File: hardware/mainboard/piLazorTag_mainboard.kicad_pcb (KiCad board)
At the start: 2 copper layers, 11 parts, among them M1 LOGIC_LEVEL_CONVERTER

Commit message: #9 More work on the mainboard
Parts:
- moved 5V_POWER1 14.0 mm to (163.8, 111.2)
- moved SSD1603 7.20 mm to (110.0, 121.6)
- moved INPUT1 6.60 mm to (150.6, 121.6)
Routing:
- net +5V: track 29.1 -> 136.6 mm
- net /IR_SIG: track 0.00 -> 50.9 mm
- net /LED_IR_GND: track 0.00 -> 20.2 mm
- net /M_LED_DI: track 0.58 -> 14.1 mm
- net /G2/i2c: track 15.8 -> 8.67 mm
- net /G3/i2c: track 15.8 -> 8.67 mm
- net /H_LED_DI: track 0.37 -> 7.48 mm
- net /G11/spi: track 17.6 -> 10.7 mm
- net /G19: track 15.3 -> 8.60 mm
- net /G6: track 15.3 -> 8.60 mm
- net /G5: track 15.3 -> 8.88 mm
- net /G26: track 15.3 -> 8.88 mm
- net /G13: track 15.3 -> 8.88 mm
- net Net-(100K1-Pad1): track 0.20 -> 6.06 mm
- net +3V3: track 96.2 -> 92.4 mm
- added copper zone on B.Cu, net GND
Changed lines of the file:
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@@
   (general
     (links 55)
-    (no_connects 36)
-    (area 0 0 0 0)
+    (no_connects 9)
+    (area 96.495 62.695238 167.205 133.833333)
     (thickness 1.6)
     (drawings 0)
-    (tracks 46)
+    (tracks 80)
     (zones 0)
     (modules 11)
@@
     (last_trace_width 1)
     (trace_clearance 0.2)
-    (zone_clearance 0.508)
+    (zone_clearance 0.6)
     (zone_45_only no)
     (trace_min 0.2)
@@
   )
   (module Pin_Headers:Pin_Header_Straight_2x01_Pitch2.54mm (layer F.Cu)
-    (at 163.8 125.2 270)
+    (at 163.8 111.2 270)
     (descr "Through hole straight pin header, 2x01, 2.54mm pitch, double rows")
     (tags "Through hole pin header THT 2x01 2.54mm double row")
@@
   )
   (module Pin_Headers:Pin_Header_Straight_1x08_Pitch2.54mm (layer F.Cu)
-    (at 150.8 128.2 270)
+    (at 150.6 121.6 270)
     (descr "Through hole straight pin header, 1x08, 2.54mm pitch, single row")
     (tags "Through hole pin header THT 1x08 2.54mm single row")
@@
   )
   (module Pin_Headers:Pin_Header_Straight_1x04_Pitch2.54mm (layer F.Cu)
-    (at 110 128.8 270)
+    (at 110 121.6 270)
     (descr "Through hole straight pin header, 1x04, 2.54mm pitch, single row")
     (tags "Through hole pin header THT 1x04 2.54mm single row")
@@
     )
   )
-  (segment (start 163.8 125.2) (end 163.8 96.52) (width 1) (layer B.Cu) (net 1))
+  (segment (start 163.8 111.2) (end 163.8 96.52) (width 1) (layer B.Cu) (net 1) (status C00000))
+  (segment (start 163.8 96.52) (end 163.49 96.21) (width 1) (layer B.Cu) (net 1) (status C00000))
+  (segment (start 112.51 88.17) (end 112.51 87.49) (width 1) (layer B.Cu) (net 1))
+  (segment (start 137.2 87) (end 141.2 83) (width 1) (layer B.Cu) (net 1))
+  (segment (start 125 87) (end 137.2 87) (width 1) (layer B.Cu) (net 1))
+  (segment (start 123.2 85.2) (end 125 87) (width 1) (layer B.Cu) (net 1))
+  (segment (start 114.8 85.2) (end 123.2 85.2) (width 1) (layer B.Cu) (net 1))
+  (segment (start 112.51 87.49) (end 114.8 85.2) (width 1) (layer B.Cu) (net 1))
+  (segment (start 115.2 67.8) (end 126 67.8) (width 1) (layer B.Cu) (net 1))
+  (segment (start 126 67.8) (end 133 74.8) (width 1) (layer B.Cu) (net 1))
+  (segment (start 118 74.8) (end 133 74.8) (width 1) (layer B.Cu) (net 1))
+  (segment (start 133 74.8) (end 141.2 83) (width 1) (layer B.Cu) (net 1))
+  (segment (start 163.49 96.21) (end 165.19 96.21) (width 1) (layer B.Cu) (net 1))
+  (segment (start 141.4 82.8) (end 141.2 83) (width 1) (layer B.Cu) (net 1))
+  (segment (start 165.8 82.8) (end 141.4 82.8) (width 1) (layer B.Cu) (net 1))
+  (segment (start 167 84) (end 165.8 82.8) (width 1) (layer B.Cu) (net 1))
+  (segment (start 167 94.4) (end 167 84) (width 1) (layer B.Cu) (net 1))
+  (segment (start 165.19 96.21) (end 167 94.4) (width 1) (layer B.Cu) (net 1))
   (segment (start 163.8 96.52) (end 163.49 96.21) (width 1) (layer B.Cu) (net 1))
+  (segment (start 123 81.4) (end 128.66 81.4) (width 1) (layer B.Cu) (net 3))
   (segment (start 128.66 81.4) (end 128.8 81.54) (width 1) (layer B.Cu) (net 3))
-  (segment (start 145.71 96.21) (end 145.71 88.59) (width 1) (layer B.Cu) (net 6) (status C00000))
-  (segment (start 112.51 98.33) (end 112.51 97.69) (width 1) (layer B.Cu) (net 6) (status C00000))
-  (segment (start 112.51 97.69) (end 113.99 96.21) (width 1) (layer B.Cu) (net 6) (status 400000))
-  (segment (start 113.99 96.21) (end 145.71 96.21) (width 1) (layer B.Cu) (net 6) (status 800000))
-  (segment (start 99.8 113) (end 97.6 113) (width 1) (layer B.Cu) (net 6) (status 400000))
-  (segment (start 109.78 95.6) (end 112.51 98.33) (width 1) (layer B.Cu) (net 6) (status 800000))
+  (segment (start 128.66 81.4) (end 128.8 81.54) (width 1) (layer B.Cu) (net 3))
+  (segment (start 128.8 79) (end 114.58 79) (width 1) (layer B.Cu) (net 4))
+  (segment (start 114.58 79) (end 110.38 74.8) (width 1) (layer B.Cu) (net 4))
+  (segment (start 107.46 121.6) (end 107.46 119.74) (width 1) (layer B.Cu) (net 6))
+  (segment (start 115.92 117.2) (end 120.12 113) (width 1) (layer B.Cu) (net 6))
+  (segment (start 110 117.2) (end 115.92 117.2) (width 1) (layer B.Cu) (net 6))
+  (segment (start 107.46 119.74) (end 110 117.2) (width 1) (layer B.Cu) (net 6))
+  (segment (start 145.71 96.21) (end 145.71 88.59) (width 1) (layer B.Cu) (net 6))
+  (segment (start 112.51 98.33) (end 112.51 97.69) (width 1) (layer B.Cu) (net 6))
+  (segment (start 112.51 97.69) (end 113.99 96.21) (width 1) (layer B.Cu) (net 6))
+  (segment (start 113.99 96.21) (end 145.71 96.21) (width 1) (layer B.Cu) (net 6))
+  (segment (start 99.8 113) (end 97.6 113) (width 1) (layer B.Cu) (net 6))
+  (segment (start 109.78 95.6) (end 112.51 98.33) (width 1) (layer B.Cu) (net 6))
   (segment (start 102.6 95.6) (end 109.78 95.6) (width 1) (layer B.Cu) (net 6))
   (segment (start 97.2 101) (end 102.6 95.6) (width 1) (layer B.Cu) (net 6))
   (segment (start 97.2 112.6) (end 97.2 101) (width 1) (layer B.Cu) (net 6))
   (segment (start 97.6 113) (end 97.2 112.6) (width 1) (layer B.Cu) (net 6))
-  (segment (start 107.46 128.8) (end 107.46 125.66) (width 1) (layer B.Cu) (net 6) (status 400000))
-  (segment (start 107.46 125.66) (end 120.12 113) (width 1) (layer B.Cu) (net 6) (status 800000))
   (segment (start 159 106) (end 159 96.8) (width 1) (layer B.Cu) (net 8))
   (segment (start 159 96.8) (end 158.41 96.21) (width 1) (layer B.Cu) (net 8))
   (segment (start 150.79 96.21) (end 150.79 100.33) (width 1) (layer B.Cu) (net 9))
   (segment (start 150.79 100.33) (end 156.46 106) (width 1) (layer B.Cu) (net 9))
-  (segment (start 102.38 128.8) (end 102.38 113.04) (width 1) (layer B.Cu) (net 10))
+  (segment (start 102.38 121.6) (end 102.38 113.04) (width 1) (layer B.Cu) (net 10))
   (segment (start 102.38 113.04) (end 102.34 113) (width 1) (layer B.Cu) (net 10))
-  (segment (start 104.92 128.8) (end 104.92 113.04) (width 1) (layer B.Cu) (net 11))
+  (segment (start 102.38 113.04) (end 102.34 113) (width 1) (layer B.Cu) (net 10))
+  (segment (start 104.92 121.6) (end 104.92 113.04) (width 1) (layer B.Cu) (net 11))
+  (segment (start 104.92 113.04) (end 104.88 113) (width 1) (layer B.Cu) (net 11))
   (segment (start 104.92 113.04) (end 104.88 113) (width 1) (layer B.Cu) (net 11))
   (segment (start 107.43 98.33) (end 107.43 105.39) (width 1) (layer B.Cu) (net 16))
@@
   (segment (start 120.13 98.33) (end 120.13 110.45) (width 1) (layer B.Cu) (net 20))
   (segment (start 120.13 110.45) (end 120.12 110.46) (width 1) (layer B.Cu) (net 20))
-  (segment (start 133.02 128.2) (end 133.02 118.28) (width 1) (layer B.Cu) (net 24) (status 400000))
-  (segment (start 133.02 118.28) (end 127.74 113) (width 1) (layer B.Cu) (net 24) (status 800000))
-  (segment (start 133.02 128.2) (end 132.78 128.2) (width 1) (layer B.Cu) (net 24))
-  (segment (start 135.56 128.2) (end 135.56 113.2) (width 1) (layer B.Cu) (net 29))
+  (segment (start 127.74 113) (end 127.74 116.52) (width 1) (layer B.Cu) (net 24))
+  (segment (start 127.74 116.52) (end 132.82 121.6) (width 1) (layer B.Cu) (net 24))
+  (segment (start 135.36 121.6) (end 135.36 113) (width 1) (layer B.Cu) (net 29))
   (segment (start 135.56 113.2) (end 135.36 113) (width 1) (layer B.Cu) (net 29))
-  (segment (start 137.9 113) (end 137.9 128) (width 1) (layer B.Cu) (net 30))
-  (segment (start 137.9 128) (end 138.1 128.2) (width 1) (layer B.Cu) (net 30))
-  (segment (start 140.64 128.2) (end 140.64 113.2) (width 1) (layer B.Cu) (net 32))
+  (segment (start 137.9 121.6) (end 137.9 113) (width 1) (layer B.Cu) (net 30))
+  (segment (start 140.44 121.6) (end 140.44 113) (width 1) (layer B.Cu) (net 32))
   (segment (start 140.64 113.2) (end 140.44 113) (width 1) (layer B.Cu) (net 32))
-  (segment (start 142.98 113) (end 142.98 128) (width 1) (layer B.Cu) (net 33))
-  (segment (start 142.98 128) (end 143.18 128.2) (width 1) (layer B.Cu) (net 33))
-  (segment (start 145.72 128.2) (end 145.72 113.2) (width 1) (layer B.Cu) (net 35))
+  (segment (start 142.98 121.6) (end 142.98 113) (width 1) (layer B.Cu) (net 33))
+  (segment (start 145.52 121.6) (end 145.52 113) (width 1) (layer B.Cu) (net 35))
   (segment (start 145.72 113.2) (end 145.52 113) (width 1) (layer B.Cu) (net 35))
   (segment (start 148.06 110.46) (end 148.06 96.4) (width 1) (layer B.Cu) (net 37))
   (segment (start 148.06 96.4) (end 148.25 96.21) (width 1) (layer B.Cu) (net 37))
+  (segment (start 107.58 67.8) (end 107.58 65.18) (width 1) (layer B.Cu) (net 38))
+  (segment (start 115.16 90.6) (end 117.59 88.17) (width 1) (layer B.Cu) (net 38))
+  (segment (start 103.8 90.6) (end 115.16 90.6) (width 1) (layer B.Cu) (net 38))
+  (segment (start 101.4 88.2) (end 103.8 90.6) (width 1) (layer B.Cu) (net 38))
+  (segment (start 101.4 65) (end 101.4 88.2) (width 1) (layer B.Cu) (net 38))
+  (segment (start 102.2 64.2) (end 101.4 65) (width 1) (layer B.Cu) (net 38))
+  (segment (start 106.6 64.2) (end 102.2 64.2) (width 1) (layer B.Cu) (net 38))
+  (segment (start 107.58 65.18) (end 106.6 64.2) (width 1) (layer B.Cu) (net 38))
+  (segment (start 105.3 74.8) (end 105.3 68.06) (width 1) (layer B.Cu) (net 39))
   (segment (start 105.3 68.06) (end 105.04 67.8) (width 1) (layer B.Cu) (net 39))
+  (segment (start 105.3 68.06) (end 105.04 67.8) (width 1) (layer B.Cu) (net 39))
+  (segment (start 107.43 88.17) (end 107.43 75.21) (width 1) (layer B.Cu) (net 45))
   (segment (start 107.43 75.21) (end 107.84 74.8) (width 1) (layer B.Cu) (net 45))
+  (segment (start 107.43 75.21) (end 107.84 74.8) (width 1) (layer B.Cu) (net 45))
+  (zone (net 2) (net_name GND) (layer B.Cu) (hatch edge 0.508)
+    (connect_pads yes (clearance 0.6))
+    (min_thickness 0.254)
+    (fill yes (arc_segments 16) (thermal_gap 0.6) (thermal_bridge_width 1))
+    (polygon
+      (pts
+        (xy 82.2 54.2) (xy 180 52.4) (xy 169.6 144) (xy 82.2 142.8)
+      )
+    )
+  )
 )

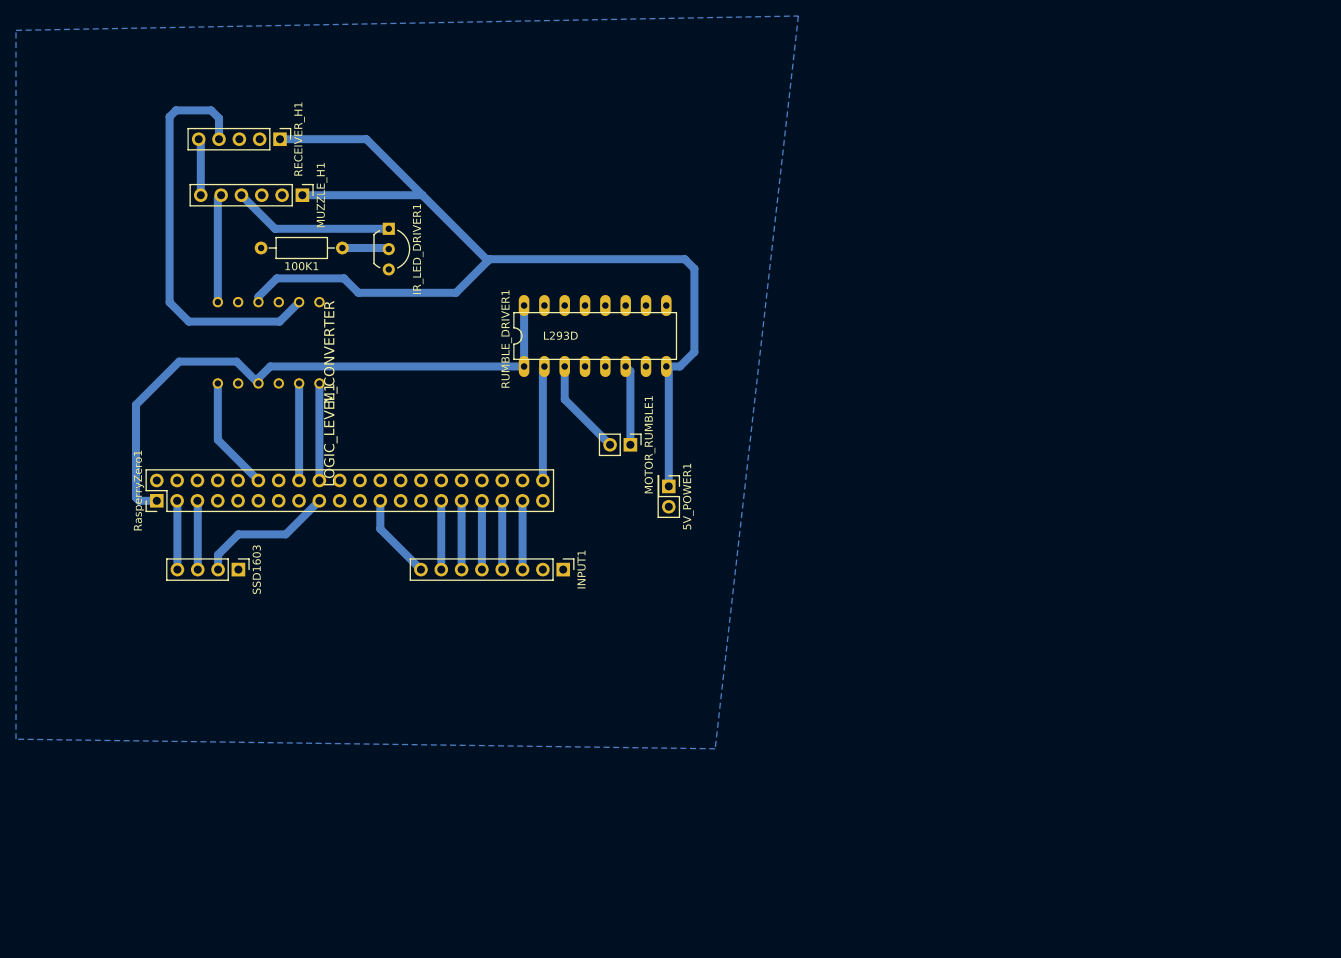
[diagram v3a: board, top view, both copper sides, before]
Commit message: #9 first Mainbaordlayout done
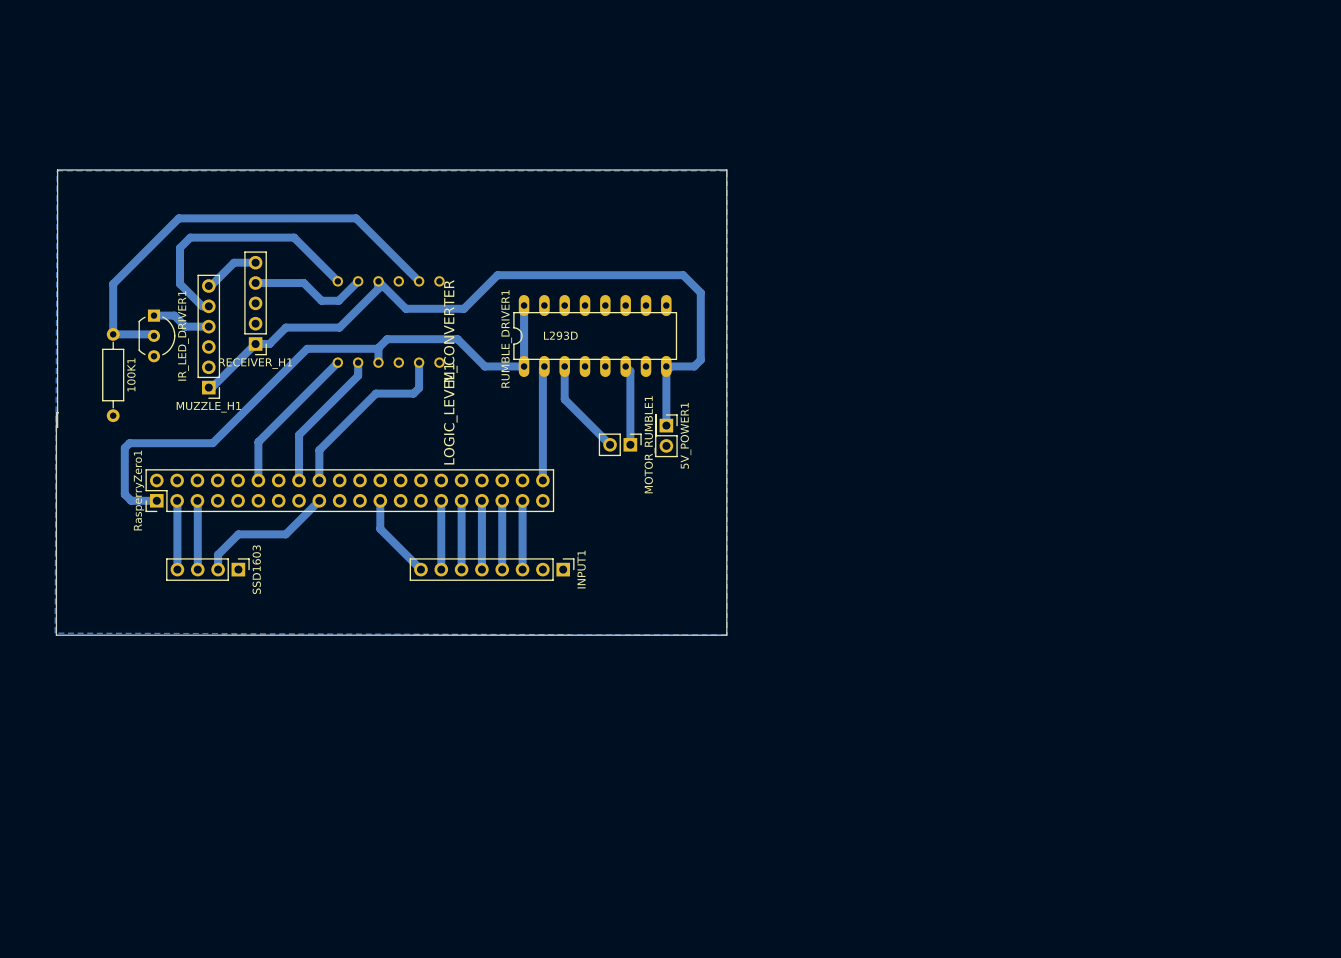
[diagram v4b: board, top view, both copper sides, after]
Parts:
- moved IR_LED_DRIVER1 31.3 mm to (99.5, 89.8)
- moved 100K1 30.6 mm to (94.3, 92.2), turned to 270 degrees
- moved MUZZLE_H1 26.7 mm to (106.3, 98.8), turned to 180 degrees
- moved RECEIVER_H1 25.8 mm to (112.2, 93.4), turned to 180 degrees
- moved M1 15.2 mm to (136.4, 97.0)
- moved 5V_POWER1 7.61 mm to (163.5, 103.6)
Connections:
- M1 pad P$11: Net-(M1-PadP$11) -> /IR_SIG
- M1 pad P$2: Net-(M1-PadP$2) -> /G23
- M1 pad P$5: /G23 -> /G24
- M1 pad P$6: /G24 -> Net-(M1-PadP$6)
- M1 pad P$7: Net-(100K1-Pad1) -> Net-(M1-PadP$7)
- M1 pad P$8: /IR_SIG -> Net-(100K1-Pad1)
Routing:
- net Net-(100K1-Pad1): track 6.06 -> 56.4 mm
- net +5V: track 136.6 -> 93.5 mm
- net /IR_SIG: track 50.9 -> 14.7 mm
- net /M_LED_DI: track 14.1 -> 31.8 mm
- net /LED_IR_GND: track 20.2 -> 7.42 mm
- net /G24: track 12.1 -> 22.7 mm
- net /G23: track 12.1 -> 17.8 mm
- net /G18: track 14.2 -> 19.1 mm
- net +3V3: track 92.4 -> 93.8 mm
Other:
- board outline added: 83.8 x 58.2 mm
